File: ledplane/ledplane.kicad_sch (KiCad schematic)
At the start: 41 parts

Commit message: Update ledplane
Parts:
- D1, D10, D11, D12, D13, D14, D15, D16, D2, D3, D4, D5, D6, D7, D8, D9: footprint LED_SMD:LED_1W_3W_R8 -> misc:LED_3W_OTDIODE
- renumbered H3 to H10, H6 to H11, H7 to H12, H9 to H13, H10 to H14, H13 to H15, H4 to H3, H5 to H4, H8 to H5, H11 to H6, H12 to H7, H14 to H8, H15 to H9

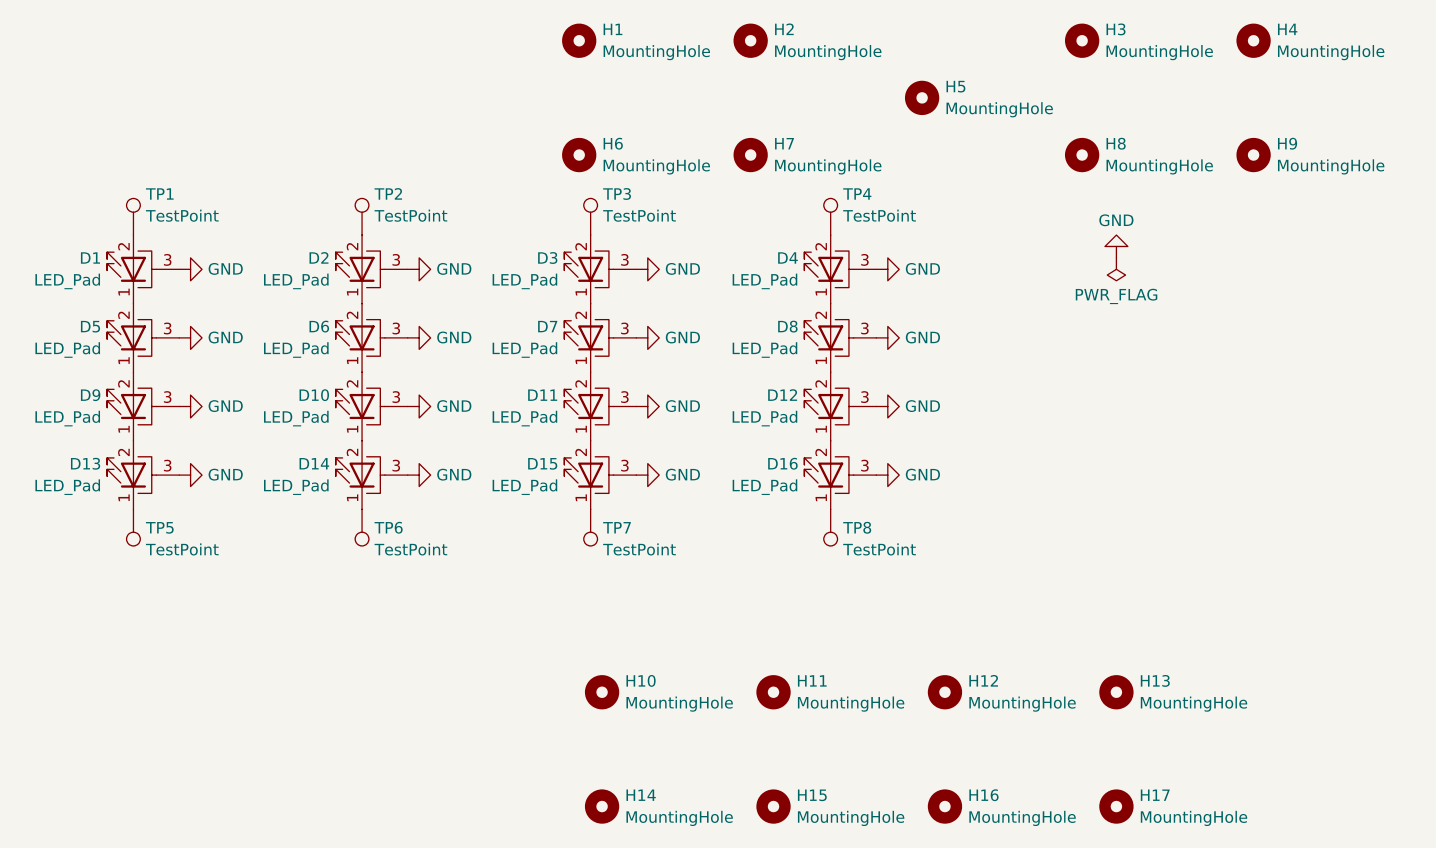
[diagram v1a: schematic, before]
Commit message: Fix bugs (gerbers not updated)
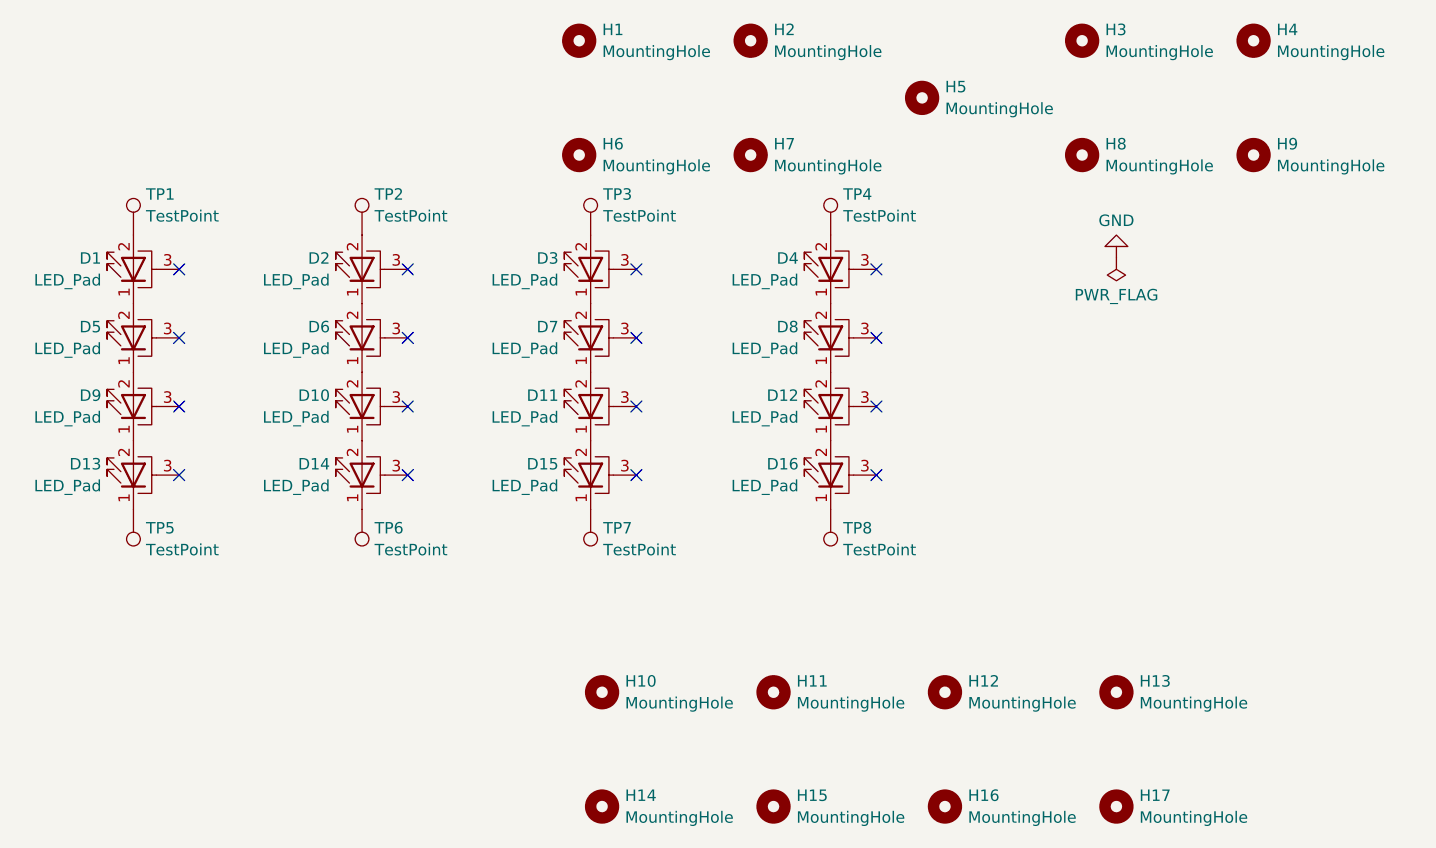
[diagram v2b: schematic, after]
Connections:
- net GND: no longer D1.3 (PAD), D10.3 (PAD), D11.3 (PAD), D12.3 (PAD), D13.3 (PAD), D14.3 (PAD), D15.3 (PAD), D16.3 (PAD), D2.3 (PAD), D3.3 (PAD), D4.3 (PAD), D5.3 (PAD), D6.3 (PAD), D7.3 (PAD), D8.3 (PAD), D9.3 (PAD)
- no-connect marks 0 -> 16

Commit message: Update ledplane
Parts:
- D1, D10, D11, D12, D13, D14, D15, D16, D2, D3, D4, D5, D6, D7, D8, D9: footprint misc:LED_3W_OTDIODE -> misc:LED_3W_OTDIODE_COMBINED
- TP1, TP2, TP3, TP4, TP5, TP6, TP7, TP8: footprint Connector_Wire:SolderWirePad_1x01_SMD_5x10mm -> misc:SolderWirePad_1x01_SMD_4x6mm
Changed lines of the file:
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@@
 			)
 		)
-		(property "Footprint" "misc:LED_3W_OTDIODE"
+		(property "Footprint" "misc:LED_3W_OTDIODE_COMBINED"
 			(at 135.89 97.79 0)
 			(effects
@@
 			)
 		)
-		(property "Footprint" "misc:LED_3W_OTDIODE"
+		(property "Footprint" "misc:LED_3W_OTDIODE_COMBINED"
 			(at 109.22 97.79 0)
 			(effects
@@
 			)
 		)
-		(property "Footprint" "misc:LED_3W_OTDIODE"
+		(property "Footprint" "misc:LED_3W_OTDIODE_COMBINED"
 			(at 58.42 74.93 0)
 			(effects
@@
 			)
 		)
-		(property "Footprint" "misc:LED_3W_OTDIODE"
+		(property "Footprint" "misc:LED_3W_OTDIODE_COMBINED"
 			(at 83.82 82.55 0)
 			(effects
@@
 			)
 		)
-		(property "Footprint" "misc:LED_3W_OTDIODE"
+		(property "Footprint" "misc:LED_3W_OTDIODE_COMBINED"
 			(at 83.82 90.17 0)
 			(effects
@@
 			)
 		)
-		(property "Footprint" "Connector_Wire:SolderWirePad_1x01_SMD_5x10mm"
+		(property "Footprint" "misc:SolderWirePad_1x01_SMD_4x6mm"
 			(at 53.34 101.6 0)
 			(effects
@@
 			)
 		)
-		(property "Footprint" "misc:LED_3W_OTDIODE"
+		(property "Footprint" "misc:LED_3W_OTDIODE_COMBINED"
 			(at 135.89 90.17 0)
 			(effects
@@
 			)
 		)
-		(property "Footprint" "Connector_Wire:SolderWirePad_1x01_SMD_5x10mm"
+		(property "Footprint" "misc:SolderWirePad_1x01_SMD_4x6mm"
 			(at 104.14 101.6 0)
 			(effects
@@
 			)
 		)
-		(property "Footprint" "Connector_Wire:SolderWirePad_1x01_SMD_5x10mm"
+		(property "Footprint" "misc:SolderWirePad_1x01_SMD_4x6mm"
 			(at 114.3 71.12 0)
 			(effects
@@
 			)
 		)
-		(property "Footprint" "misc:LED_3W_OTDIODE"
+		(property "Footprint" "misc:LED_3W_OTDIODE_COMBINED"
 			(at 135.89 74.93 0)
 			(effects
@@
 			)
 		)
-		(property "Footprint" "misc:LED_3W_OTDIODE"
+		(property "Footprint" "misc:LED_3W_OTDIODE_COMBINED"
 			(at 58.42 97.79 0)
 			(effects
@@
 			)
 		)
-		(property "Footprint" "misc:LED_3W_OTDIODE"
+		(property "Footprint" "misc:LED_3W_OTDIODE_COMBINED"
 			(at 135.89 82.55 0)
 			(effects
@@
 			)
 		)
-		(property "Footprint" "Connector_Wire:SolderWirePad_1x01_SMD_5x10mm"
+		(property "Footprint" "misc:SolderWirePad_1x01_SMD_4x6mm"
 			(at 140.97 71.12 0)
 			(effects
@@
 			)
 		)
-		(property "Footprint" "Connector_Wire:SolderWirePad_1x01_SMD_5x10mm"
+		(property "Footprint" "misc:SolderWirePad_1x01_SMD_4x6mm"
 			(at 130.81 101.6 0)
 			(effects
@@
 			)
 		)
-		(property "Footprint" "misc:LED_3W_OTDIODE"
+		(property "Footprint" "misc:LED_3W_OTDIODE_COMBINED"
 			(at 109.22 90.17 0)
 			(effects
@@
 			)
 		)
-		(property "Footprint" "misc:LED_3W_OTDIODE"
+		(property "Footprint" "misc:LED_3W_OTDIODE_COMBINED"
 			(at 109.22 82.55 0)
 			(effects
@@
 			)
 		)
-		(property "Footprint" "Connector_Wire:SolderWirePad_1x01_SMD_5x10mm"
+		(property "Footprint" "misc:SolderWirePad_1x01_SMD_4x6mm"
 			(at 63.5 71.12 0)
 			(effects
@@
 			)
 		)
-		(property "Footprint" "misc:LED_3W_OTDIODE"
+		(property "Footprint" "misc:LED_3W_OTDIODE_COMBINED"
 			(at 58.42 90.17 0)
 			(effects
@@
 			)
 		)
-		(property "Footprint" "misc:LED_3W_OTDIODE"
+		(property "Footprint" "misc:LED_3W_OTDIODE_COMBINED"
 			(at 109.22 74.93 0)
 			(effects
@@
 			)
 		)
-		(property "Footprint" "Connector_Wire:SolderWirePad_1x01_SMD_5x10mm"
+		(property "Footprint" "misc:SolderWirePad_1x01_SMD_4x6mm"
 			(at 78.74 101.6 0)
 			(effects
@@
 			)
 		)
-		(property "Footprint" "misc:LED_3W_OTDIODE"
+		(property "Footprint" "misc:LED_3W_OTDIODE_COMBINED"
 			(at 83.82 97.79 0)
 			(effects
@@
 			)
 		)
-		(property "Footprint" "misc:LED_3W_OTDIODE"
+		(property "Footprint" "misc:LED_3W_OTDIODE_COMBINED"
 			(at 83.82 74.93 0)
 			(effects
@@
 			)
 		)
-		(property "Footprint" "misc:LED_3W_OTDIODE"
+		(property "Footprint" "misc:LED_3W_OTDIODE_COMBINED"
 			(at 58.42 82.55 0)
 			(effects
@@
 			)
 		)
-		(property "Footprint" "Connector_Wire:SolderWirePad_1x01_SMD_5x10mm"
+		(property "Footprint" "misc:SolderWirePad_1x01_SMD_4x6mm"
 			(at 88.9 71.12 0)
 			(effects
